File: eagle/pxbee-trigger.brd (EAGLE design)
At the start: 51 x 57 mm, 21 parts, among them J1 39501-1002, J2 39501-1009, K1 APAN3103, K2 APAN3103, K3 APAN3103, K4 APAN3103, Q1 BC548BTA, Q2 BC548BTA, Q3 BC548BTA, Q4 BC548BTA

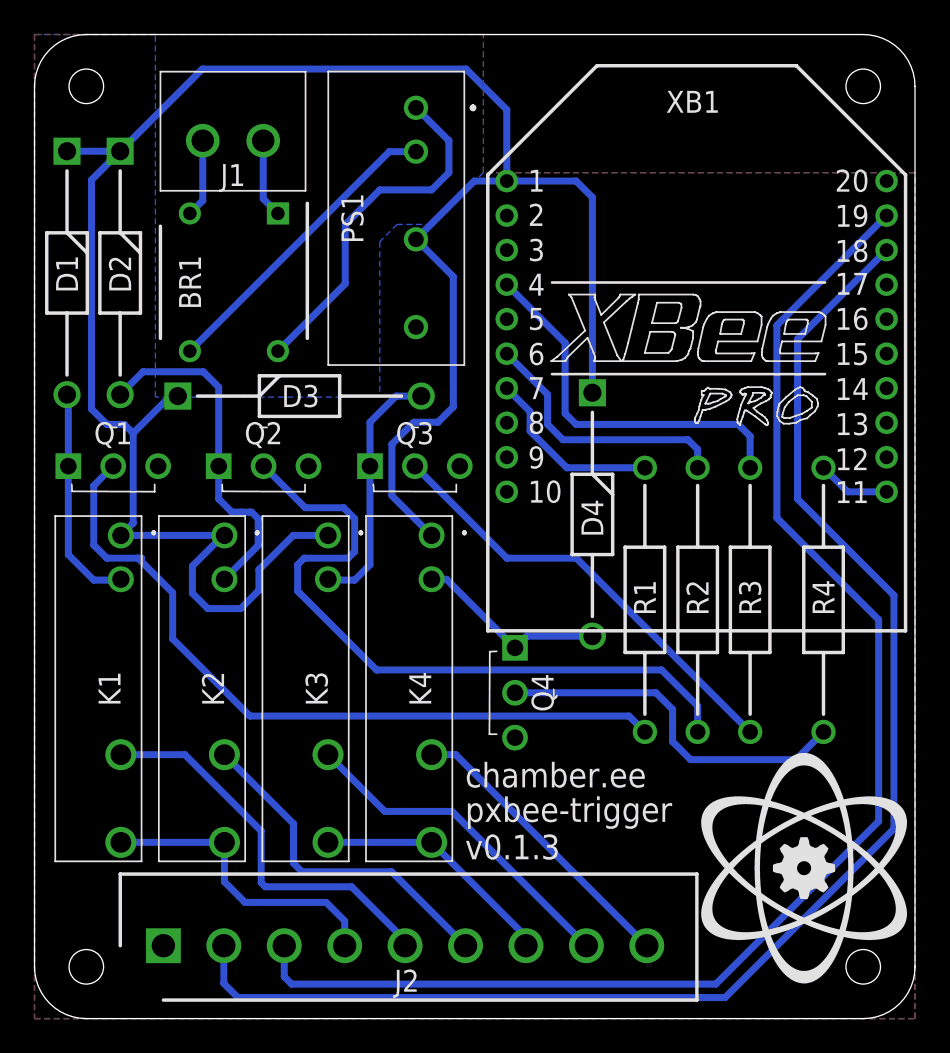
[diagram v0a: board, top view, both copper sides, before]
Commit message: Added capacitors for fixing #12
- Version of the PCB updated to v0.3.0
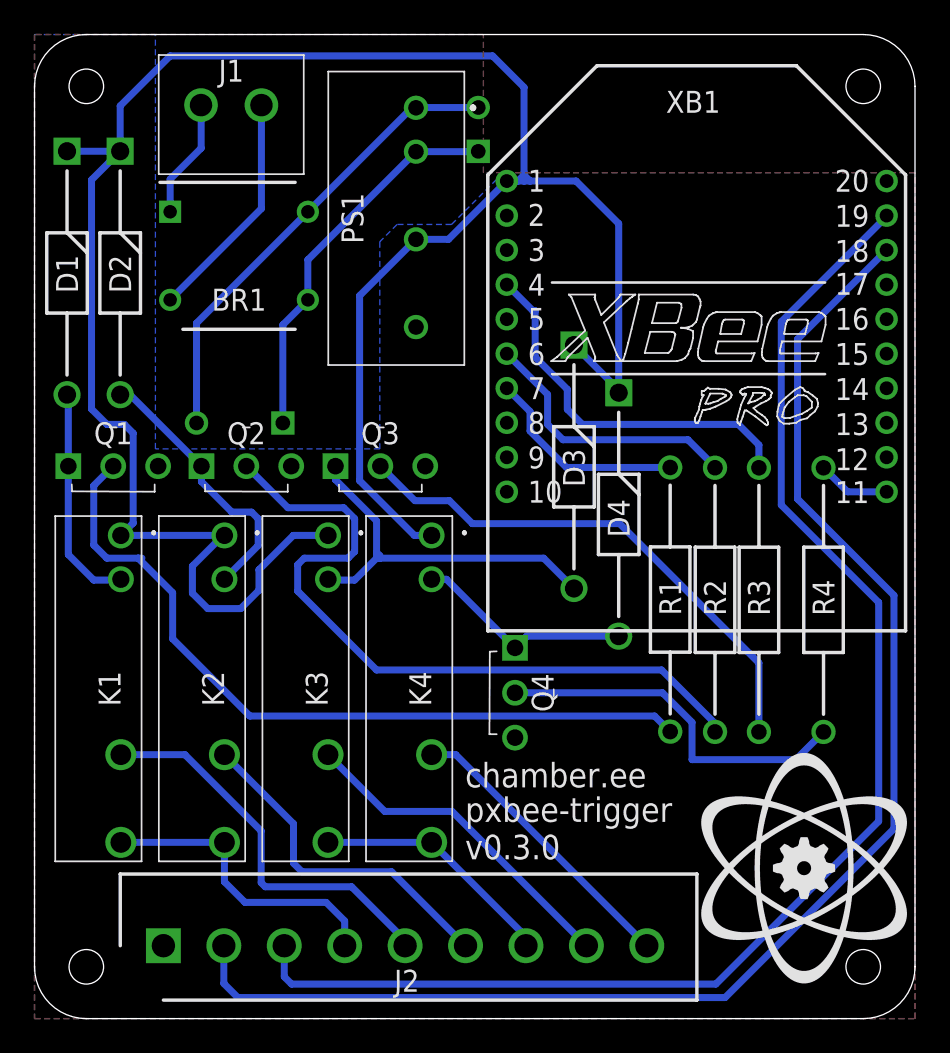
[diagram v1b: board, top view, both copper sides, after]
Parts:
- added C1: EEU-FM1H221-A, parts:CAPANGLED
- added C2: EEU-FM1H221-A2, parts:CAPANGLED-B
- moved D3 23.1 mm to (31.2, 39.0), turned to 270 degrees
- moved J1 3.97 mm to (13.1, 52.9), turned to 180 degrees
- moved Q3 2.00 mm to (17.4, 32.0)
- moved BR1 1.56 mm to (11.8, 44.2), turned to 0 degrees
- moved D4 1.52 mm to (33.8, 36.3)
- moved R1 1.47 mm to (36.8, 16.6)
- moved R2 1.01 mm to (39.4, 16.6)
- moved Q2 1.00 mm to (9.67, 32.0)
- moved R3 0.51 mm to (42.0, 16.6)
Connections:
- removed net N$10: BR1.4, PS1.1
- removed net N$11: BR1.3, PS1.2
- new net VIN+: BR1.3, C1.1, C2.1, PS1.2
- new net VIN-: BR1.4, C1.2, C2.2, PS1.1
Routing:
- net VIN-: track 0.00 -> 27.3 mm
- net VIN+: track 0.00 -> 22.5 mm
- net N$10: track 20.7 -> 0.00 mm
- net N$11: track 17.9 -> 0.00 mm
- net N$9: track 4.52 -> 13.5 mm
- net N$6: track 14.7 -> 22.2 mm
- net VCC: track 126.2 -> 131.7 mm
- net N$5: track 25.8 -> 30.6 mm
- net N$4: track 20.2 -> 15.8 mm
- net N$8: track 4.57 -> 6.93 mm
- net N$12: track 11.2 -> 12.8 mm
- net N$13: track 10.6 -> 12.0 mm
- net N$1: track 43.2 -> 44.7 mm
- net N$2: track 41.0 -> 42.4 mm
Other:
- board text added: "v0.3.0"
- board text removed: "v0.1.3"

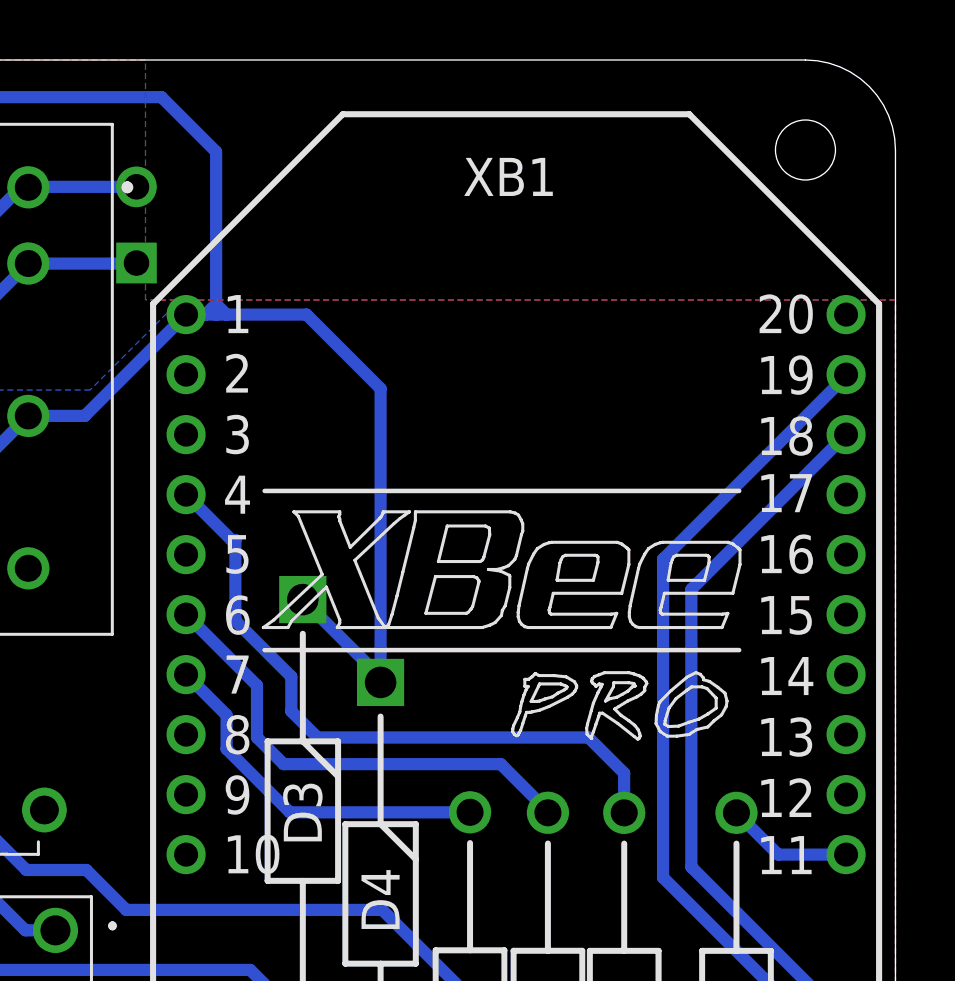
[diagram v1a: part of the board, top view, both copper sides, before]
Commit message: UART header added for easier debugging
- Fixes #13
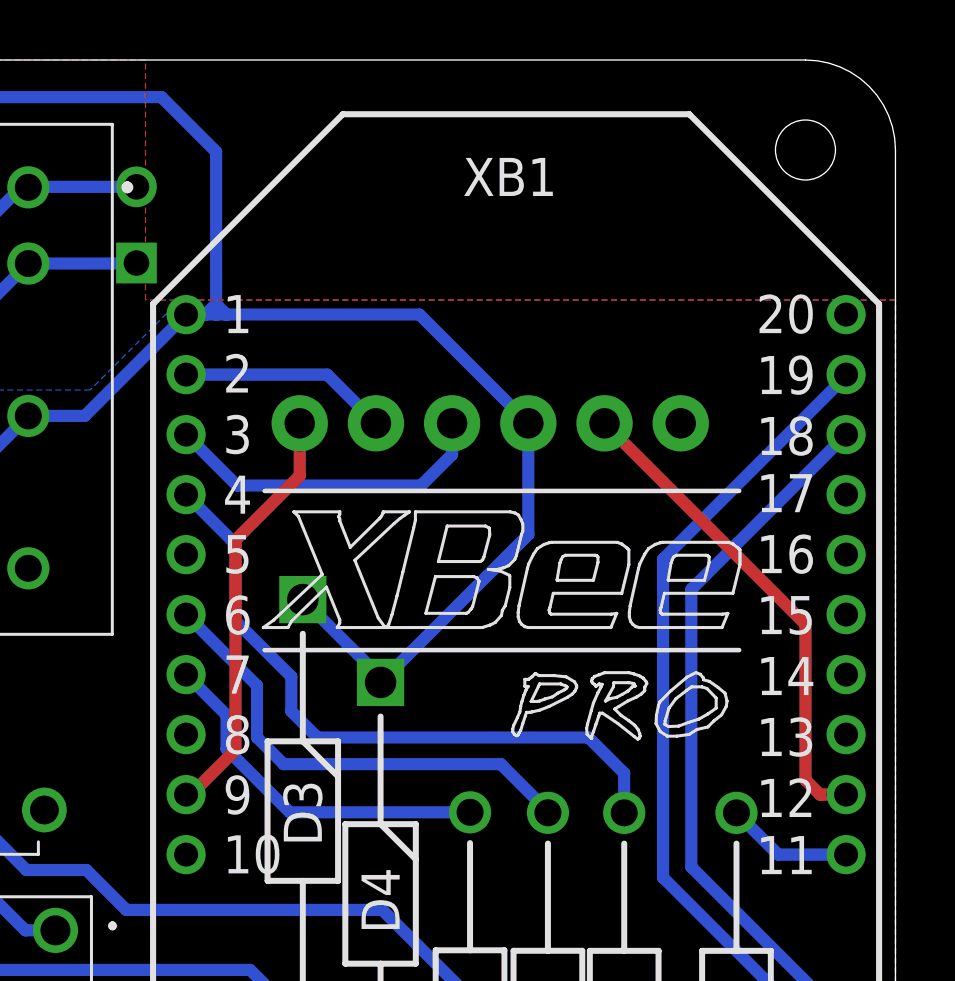
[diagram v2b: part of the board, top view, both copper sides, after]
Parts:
- added JP1: (no value), SparkFun-Connectors:6_PIN_SERIAL_TARGET_SIDE_W_SILK
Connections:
- new net CTS: JP1.P$5, XB1.12
- new net DTR: JP1.P$1, XB1.9
- new net RXI: JP1.P$3, XB1.3
- new net TXO: JP1.P$2, XB1.2
- net GND: now also JP1.P$6
- net VCC: now also JP1.P$4
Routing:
- net CTS: track 0.00 -> 16.2 mm
- net DTR: track 0.00 -> 14.0 mm
- net RXI: track 0.00 -> 11.1 mm
- net TXO: track 0.00 -> 7.00 mm
- net VCC: track 131.7 -> 138.0 mm

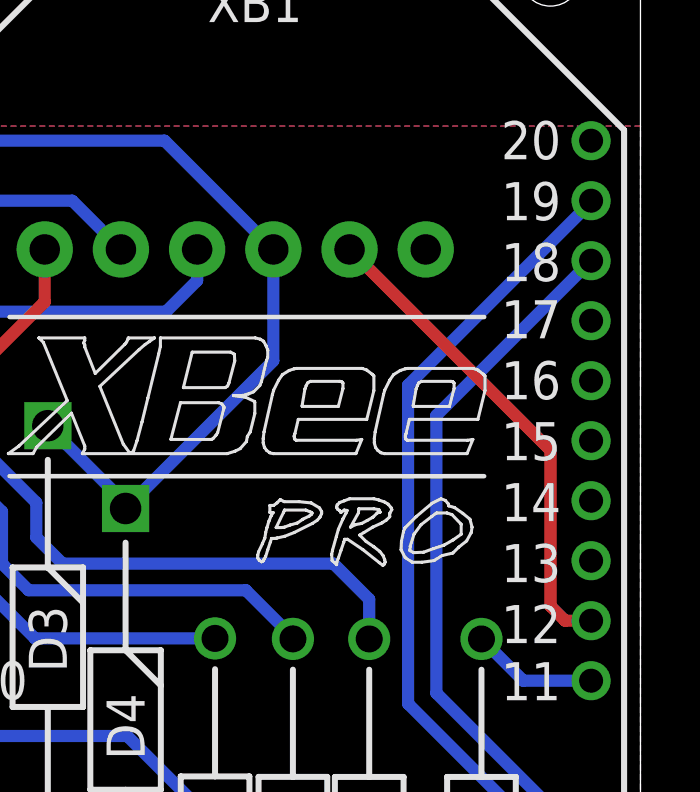
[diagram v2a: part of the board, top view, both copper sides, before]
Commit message: Change CTS routing on PCB
- Further contributes to #13
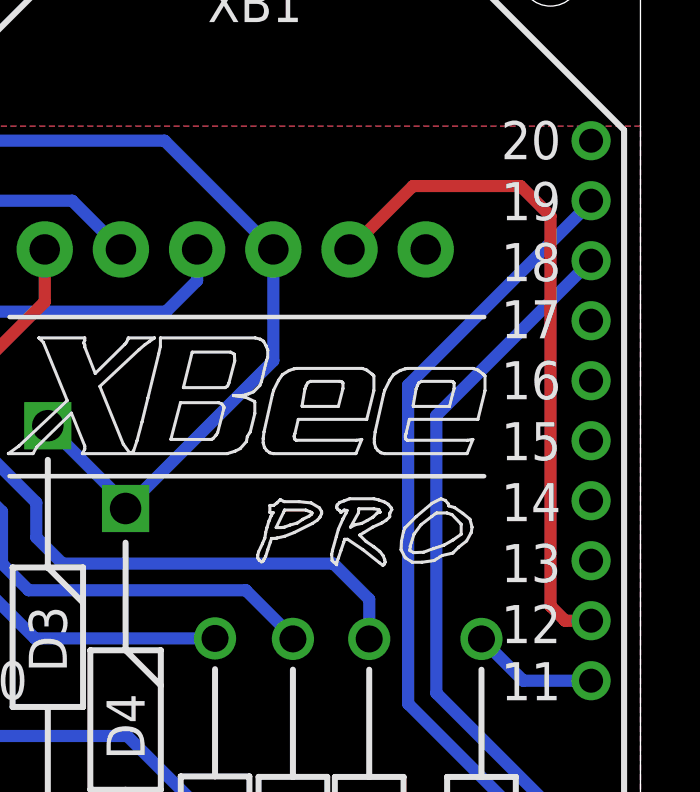
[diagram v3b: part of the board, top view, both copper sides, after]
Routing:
- net CTS: track 16.2 -> 22.5 mm
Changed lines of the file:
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@@
 <contactref element="XB1" pad="12"/>
 <contactref element="JP1" pad="P$5"/>
-<wire x1="41.302" y1="44.889" x2="48" y2="38.191" width="0.4064" layer="1"/>
-<wire x1="48" y1="38.191" x2="48" y2="33" width="0.4064" layer="1"/>
 <wire x1="48" y1="33" x2="48.487" y2="32.513" width="0.4064" layer="1"/>
 <wire x1="48.487" y1="32.513" x2="49.354" y2="32.513" width="0.4064" layer="1"/>
+<wire x1="41.302" y1="44.889" x2="43.413" y2="47" width="0.4064" layer="1"/>
+<wire x1="47" y1="47" x2="48" y2="46" width="0.4064" layer="1"/>
+<wire x1="43.413" y1="47" x2="47" y2="47" width="0.4064" layer="1"/>
+<wire x1="48" y1="46" x2="48" y2="33" width="0.4064" layer="1"/>
 </signal>
 <signal name="TXO">
